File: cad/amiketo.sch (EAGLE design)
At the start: 58 parts, among them CN1 MICROSDPLAIN, J1 HEADER-5X1, Q1 IRLML6344TRPBF, Q2 DMP2035U-7, SW2 SWITCHKMR211, SW3 SWITCHKMR211, U1 STM32F411/48, U2 LSM303D, U3 ADP5062, U4 MCP1824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

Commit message: lis3dh accel
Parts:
- removed C12: 4.7u, jaw:C0603
- removed C13: .22u, jaw:C0603
- U2: value LSM303D -> LIS3DH; device jaw:LSM303D -> jaw:LIS3DH
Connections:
- removed net N$1: C12.P$1, U2.C1
- removed net N$2: C13.P$2, U2.SETP
- removed net N$4: C13.P$1, U2.SETC
- net GND: no longer C12.P$2
- net VCC: now also U2.VCC; no longer U2.VDD
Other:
- moved on the sheet: U2
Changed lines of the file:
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@@
 <part name="U$2" library="adafruit" deviceset="FIDUCIAL" device=""/>
 <part name="U$3" library="adafruit" deviceset="FIDUCIAL" device=""/>
-<part name="C12" library="jaw" deviceset="C" device="0603" value="4.7u"/>
-<part name="C13" library="jaw" deviceset="C" device="0603" value=".22u"/>
 <part name="C14" library="jaw" deviceset="C" device="0603" value=".1u"/>
 <part name="GND12" library="jaw" deviceset="PWR-GND" device=""/>
@@
 <part name="B1" library="jaw" deviceset="BATTERY" device="-CR2016"/>
 <part name="X1" library="jaw" deviceset="RESONATOR" device="CTCE" value="12MHz"/>
-<part name="U2" library="jaw" deviceset="LSM303D" device=""/>
 <part name="U5" library="jaw" deviceset="MAX17048" device=""/>
 <part name="LOGO1" library="Sparkfun-Aesthetics" deviceset="OSHW-LOGO" device="M"/>
@@
 <part name="C6" library="jaw" deviceset="C" device="0603" value="1u"/>
 <part name="C7" library="jaw" deviceset="C" device="0603" value="1u"/>
+<part name="U2" library="jaw" deviceset="LIS3DH" device=""/>
 </parts>
 <sheets>
@@
 <instance part="U$2" gate="G$1" x="269.24" y="40.64"/>
 <instance part="U$3" gate="G$1" x="261.62" y="40.64"/>
-<instance part="C12" gate="G$1" x="127" y="109.22" rot="R90"/>
-<instance part="C13" gate="G$1" x="124.46" y="101.6" rot="R90"/>
 <instance part="C14" gate="G$1" x="132.08" y="119.38"/>
 <instance part="GND12" gate="G$1" x="99.06" y="81.28"/>
@@
 <instance part="B1" gate="G$1" x="226.06" y="170.18"/>
 <instance part="X1" gate="G$1" x="144.78" y="160.02"/>
-<instance part="U2" gate="G$1" x="99.06" y="106.68"/>
 <instance part="U5" gate="G$1" x="127" y="25.4"/>
 <instance part="LOGO1" gate="G$1" x="203.2" y="45.72"/>
@@
 <instance part="C6" gate="G$1" x="226.06" y="73.66"/>
 <instance part="C7" gate="G$1" x="226.06" y="165.1" rot="R270"/>
+<instance part="U2" gate="G$1" x="99.06" y="106.68"/>
 </instances>
 <busses>
@@
 <pinref part="GND12" gate="G$1" pin="GND"/>
 <wire x1="99.06" y1="88.9" x2="99.06" y2="86.36" width="0.1524" layer="91"/>
+<wire x1="99.06" y1="86.36" x2="99.06" y2="83.82" width="0.1524" layer="91"/>
 <pinref part="U2" gate="G$1" pin="GND"/>
-<wire x1="99.06" y1="86.36" x2="99.06" y2="83.82" width="0.1524" layer="91"/>
-<junction x="99.06" y="86.36"/>
-</segment>
-<segment>
-<pinref part="C12" gate="G$1" pin="P$2"/>
-<wire x1="129.54" y1="109.22" x2="132.08" y2="109.22" width="0.1524" layer="91"/>
+<wire x1="99.06" y1="88.9" x2="99.06" y2="91.44" width="0.1524" layer="91"/>
+</segment>
+<segment>
 <wire x1="132.08" y1="109.22" x2="132.08" y2="96.52" width="0.1524" layer="91"/>
 <pinref part="GND14" gate="G$1" pin="GND"/>
 <wire x1="132.08" y1="96.52" x2="132.08" y2="88.9" width="0.1524" layer="91"/>
 <wire x1="132.08" y1="114.3" x2="132.08" y2="109.22" width="0.1524" layer="91"/>
-<junction x="132.08" y="109.22"/>
 <pinref part="C14" gate="G$1" pin="P$2"/>
 <wire x1="132.08" y1="116.84" x2="132.08" y2="114.3" width="0.1524" layer="91"/>
@@
 </segment>
 <segment>
-<pinref part="U2" gate="G$1" pin="SA0"/>
-<wire x1="81.28" y1="96.52" x2="76.2" y2="96.52" width="0.1524" layer="91"/>
-<label x="73.66" y="96.52" size="1.27" layer="95"/>
-</segment>
-<segment>
 <pinref part="U5" gate="G$1" pin="QSTRT"/>
 <wire x1="142.24" y1="22.86" x2="147.32" y2="22.86" width="0.1524" layer="91"/>
@@
 <pinref part="GND24" gate="G$1" pin="GND"/>
 <wire x1="264.16" y1="68.58" x2="256.54" y2="68.58" width="0.1524" layer="91"/>
+</segment>
+<segment>
+<pinref part="U2" gate="G$1" pin="SA0"/>
+<wire x1="83.82" y1="109.22" x2="78.74" y2="109.22" width="0.1524" layer="91"/>
+<label x="73.66" y="109.22" size="1.27" layer="95"/>
 </segment>
 </net>
@@
 <junction x="99.06" y="127"/>
 <pinref part="U2" gate="G$1" pin="VDDIO"/>
-<junction x="96.52" y="127"/>
-<pinref part="U2" gate="G$1" pin="VDD"/>
+<wire x1="101.6" y1="124.46" x2="101.6" y2="121.92" width="0.1524" layer="91"/>
+<pinref part="U2" gate="G$1" pin="VCC"/>
+<wire x1="96.52" y1="124.46" x2="96.52" y2="121.92" width="0.1524" layer="91"/>
 </segment>
 <segment>
@@
 <label x="246.38" y="177.8" size="1.27" layer="95"/>
 <pinref part="J1" gate="G$1" pin="1"/>
-</segment>
-<segment>
-<pinref part="U2" gate="G$1" pin="CS"/>
-<wire x1="81.28" y1="116.84" x2="76.2" y2="116.84" width="0.1524" layer="91"/>
-<label x="73.66" y="116.84" size="1.27" layer="95"/>
 </segment>
 <segment>
@@
 <wire x1="139.7" y1="78.74" x2="139.7" y2="76.2" width="0.1524" layer="91"/>
 <wire x1="139.7" y1="76.2" x2="142.24" y2="76.2" width="0.1524" layer="91"/>
+</segment>
+<segment>
+<pinref part="U2" gate="G$1" pin="CS"/>
+<wire x1="114.3" y1="104.14" x2="119.38" y2="104.14" width="0.1524" layer="91"/>
+<label x="119.38" y="104.14" size="1.27" layer="95"/>
 </segment>
 </net>
@@
 </segment>
 <segment>
-<pinref part="U2" gate="G$1" pin="SCL"/>
-<wire x1="81.28" y1="111.76" x2="76.2" y2="111.76" width="0.1524" layer="91"/>
-<label x="73.66" y="111.76" size="1.27" layer="95"/>
-</segment>
-<segment>
 <pinref part="U5" gate="G$1" pin="SCL"/>
 <wire x1="142.24" y1="27.94" x2="147.32" y2="27.94" width="0.1524" layer="91"/>
@@
 <label x="243.84" y="101.6" size="1.27" layer="95"/>
 </segment>
+<segment>
+<pinref part="U2" gate="G$1" pin="SCL"/>
+<wire x1="83.82" y1="114.3" x2="78.74" y2="114.3" width="0.1524" layer="91"/>
+<label x="73.66" y="114.3" size="1.27" layer="95"/>
+</segment>
 </net>
 <net name="I2CDA" class="0">
@@
 </segment>
 <segment>
-<pinref part="U2" gate="G$1" pin="SDA"/>
-<wire x1="81.28" y1="109.22" x2="76.2" y2="109.22" width="0.1524" layer="91"/>
-<label x="73.66" y="109.22" size="1.27" layer="95"/>
-</segment>
-<segment>
 <pinref part="U5" gate="G$1" pin="SDA"/>
 <wire x1="142.24" y1="30.48" x2="147.32" y2="30.48" width="0.1524" layer="91"/>
@@
 <label x="243.84" y="99.06" size="1.27" layer="95"/>
 </segment>
+<segment>
+<pinref part="U2" gate="G$1" pin="SDA"/>
+<wire x1="83.82" y1="111.76" x2="78.74" y2="111.76" width="0.1524" layer="91"/>
+<label x="73.66" y="111.76" size="1.27" layer="95"/>
+</segment>
 </net>
 <net name="DPYDC" class="0">
@@
 <segment>
 <pinref part="U2" gate="G$1" pin="INT1"/>
-<wire x1="81.28" y1="101.6" x2="76.2" y2="101.6" width="0.1524" layer="91"/>
-<label x="73.66" y="101.6" size="1.27" layer="95"/>
+<wire x1="114.3" y1="109.22" x2="119.38" y2="109.22" width="0.1524" layer="91"/>
+<label x="119.38" y="109.22" size="1.27" layer="95"/>
 </segment>
 </net>
@@
 </segment>
 </net>
-<net name="N$1" class="0">
-<segment>
-<pinref part="C12" gate="G$1" pin="P$1"/>
-<pinref part="U2" gate="G$1" pin="C1"/>
-<wire x1="121.92" y1="109.22" x2="114.3" y2="109.22" width="0.1524" layer="91"/>
-</segment>
-</net>
-<net name="N$2" class="0">
-<segment>
-<pinref part="U2" gate="G$1" pin="SETP"/>
-<wire x1="114.3" y1="106.68" x2="127" y2="106.68" width="0.1524" layer="91"/>
-<pinref part="C13" gate="G$1" pin="P$2"/>
-<wire x1="127" y1="106.68" x2="127" y2="101.6" width="0.1524" layer="91"/>
-</segment>
-</net>
-<net name="N$4" class="0">
-<segment>
-<pinref part="C13" gate="G$1" pin="P$1"/>
-<wire x1="119.38" y1="101.6" x2="116.84" y2="101.6" width="0.1524" layer="91"/>
-<wire x1="116.84" y1="101.6" x2="116.84" y2="104.14" width="0.1524" layer="91"/>
-<pinref part="U2" gate="G$1" pin="SETC"/>
-<wire x1="116.84" y1="104.14" x2="114.3" y2="104.14" width="0.1524" layer="91"/>
-</segment>
-</net>

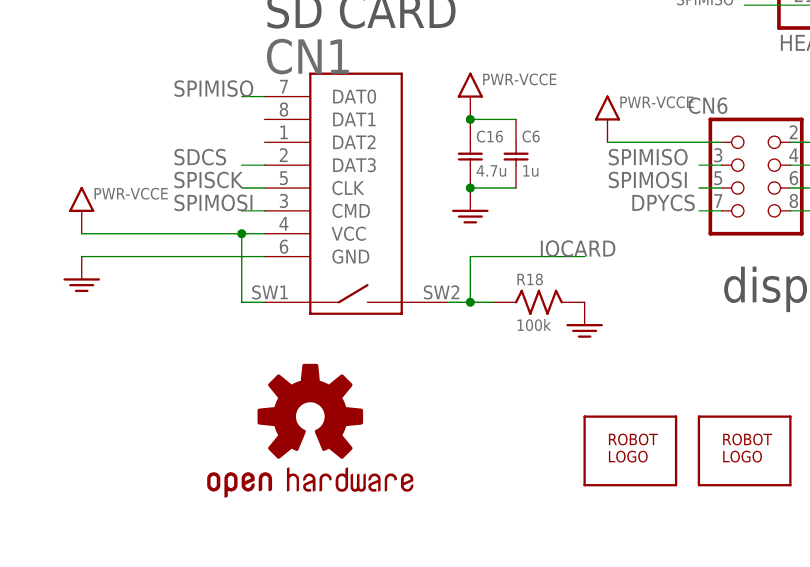
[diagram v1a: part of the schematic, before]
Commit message: move usb, embiggen sd
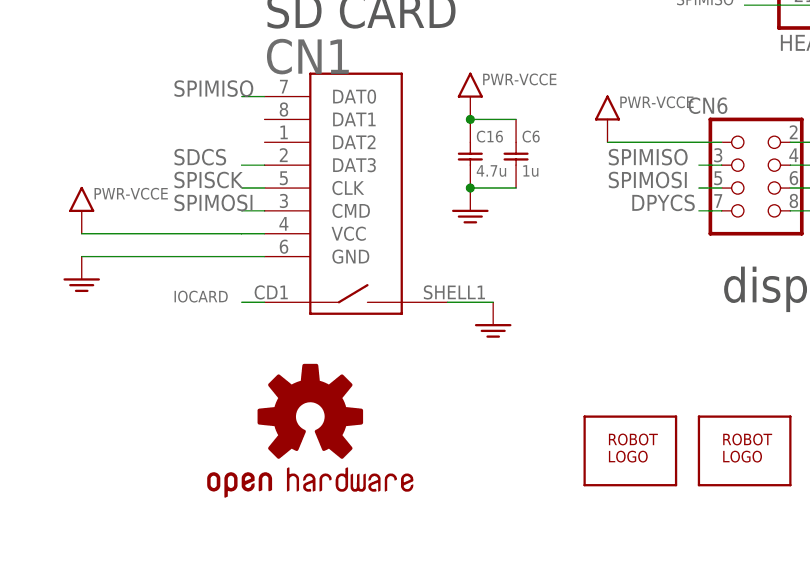
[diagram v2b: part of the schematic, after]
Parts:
- removed R18: 100k, jaw:R0603
- CN1: value MICROSDPLAIN -> MICROSD-EJECT; device jaw:MICROSDPLAIN -> jaw:MICROSD-EJECT
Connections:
- net GND: now also CN1.SW2; no longer R18.P$2
- net IOCARD: now also CN1.SW1; no longer CN1.SW2, R18.P$1
- net VCCE: no longer CN1.SW1
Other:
- moved on the sheet: CN1
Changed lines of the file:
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@@
 <part name="GND10" library="jaw" deviceset="PWR-GND" device=""/>
 <part name="Q1" library="jaw" deviceset="MOSFET" device="SOT-23" value="IRLML6344TRPBF"/>
-<part name="CN1" library="jaw" deviceset="MICROSD" device="PLAIN"/>
+<part name="CN1" library="jaw" deviceset="MICROSD" device="-EJECT" value="MICROSD-EJECT"/>
 <part name="GND22" library="jaw" deviceset="PWR-GND" device=""/>
 <part name="C16" library="jaw" deviceset="C" device="0603" value="4.7u"/>
 <part name="GND23" library="jaw" deviceset="PWR-GND" device=""/>
-<part name="R18" library="jaw" deviceset="R" device="0603" value="100k"/>
 <part name="GND13" library="jaw" deviceset="PWR-GND" device=""/>
 <part name="U$2" library="adafruit" deviceset="FIDUCIAL" device=""/>
@@
 <instance part="C16" gate="G$1" x="220.98" y="73.66"/>
 <instance part="GND23" gate="G$1" x="220.98" y="68.58"/>
-<instance part="R18" gate="G$1" x="228.6" y="58.42"/>
-<instance part="GND13" gate="G$1" x="233.68" y="55.88"/>
+<instance part="GND13" gate="G$1" x="223.52" y="55.88"/>
 <instance part="U$2" gate="G$1" x="269.24" y="40.64"/>
 <instance part="U$3" gate="G$1" x="261.62" y="40.64"/>
@@
 </segment>
 <segment>
-<pinref part="R18" gate="G$1" pin="P$2"/>
-<pinref part="GND13" gate="G$1" pin="GND"/>
-</segment>
-<segment>
 <pinref part="GND9" gate="G$1" pin="GND"/>
 <pinref part="LED1" gate="G$1" pin="C"/>
@@
 <wire x1="83.82" y1="109.22" x2="78.74" y2="109.22" width="0.1524" layer="91"/>
 <label x="73.66" y="109.22" size="1.27" layer="95"/>
+</segment>
+<segment>
+<pinref part="CN1" gate="G$1" pin="SW2"/>
+<pinref part="GND13" gate="G$1" pin="GND"/>
+<wire x1="218.44" y1="58.42" x2="223.52" y2="58.42" width="0.1524" layer="91"/>
 </segment>
 </net>
@@
 <net name="IOCARD" class="0">
 <segment>
-<pinref part="CN1" gate="G$1" pin="SW2"/>
-<pinref part="R18" gate="G$1" pin="P$1"/>
-<wire x1="218.44" y1="58.42" x2="220.98" y2="58.42" width="0.1524" layer="91"/>
-<wire x1="220.98" y1="58.42" x2="223.52" y2="58.42" width="0.1524" layer="91"/>
-<wire x1="220.98" y1="58.42" x2="220.98" y2="63.5" width="0.1524" layer="91"/>
-<junction x="220.98" y="58.42"/>
-<wire x1="220.98" y1="63.5" x2="233.68" y2="63.5" width="0.1524" layer="91"/>
-<label x="228.6" y="63.5" size="1.778" layer="95"/>
-</segment>
-<segment>
 <pinref part="U1" gate="G$1" pin="PA15"/>
 <wire x1="193.04" y1="124.46" x2="198.12" y2="124.46" width="0.1524" layer="91"/>
 <label x="198.12" y="124.46" size="1.27" layer="95"/>
+</segment>
+<segment>
+<pinref part="CN1" gate="G$1" pin="SW1"/>
+<wire x1="198.12" y1="58.42" x2="195.58" y2="58.42" width="0.1524" layer="91"/>
+<label x="187.96" y="58.42" size="1.27" layer="95"/>
 </segment>
 </net>
@@
 <pinref part="CN1" gate="G$1" pin="VCC"/>
 <wire x1="177.8" y1="66.04" x2="195.58" y2="66.04" width="0.1524" layer="91"/>
-<pinref part="CN1" gate="G$1" pin="SW1"/>
 <wire x1="195.58" y1="66.04" x2="198.12" y2="66.04" width="0.1524" layer="91"/>
-<wire x1="198.12" y1="58.42" x2="195.58" y2="58.42" width="0.1524" layer="91"/>
-<wire x1="195.58" y1="58.42" x2="195.58" y2="66.04" width="0.1524" layer="91"/>
-<junction x="195.58" y="66.04"/>
 <pinref part="VCCE2" gate="G$1" pin="VCCE"/>
 </segment>

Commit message: 22pin connector
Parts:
- added C12: .1u, jaw:C0603
- JP1: value HEADER-21X1 -> HEADER-22X1-PTH; device jaw:HEADER-21X1 -> jaw:HEADER-22X1-PTH
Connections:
- net BOOT0: now also JP1.16; no longer JP1.15
- net GND: now also C12.P$2, JP1.13; no longer JP1.12
- net I2CCL: now also JP1.18; no longer JP1.17
- net I2CDA: now also JP1.19; no longer JP1.18
- net NRST: now also JP1.17; no longer JP1.16
- net RX: now also JP1.14; no longer JP1.13
- net SPIMISO: now also JP1.22; no longer JP1.21
- net SPIMOSI: now also JP1.21; no longer JP1.20
- net SPISCK: now also JP1.20; no longer JP1.19
- net TX: now also JP1.15; no longer JP1.14
- net VCC: now also C12.P$1
- net VUSB: now also JP1.12

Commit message: tweak, silk
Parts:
- C6: value 1u -> .1u
- F1: value (none) -> FUSE; device adafruit:PTCFUSE-1206 -> jaw:FUSE
- renumbered NOISY1 to SPKR1
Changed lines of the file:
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@@
 <part name="USB1" library="dp_devices" deviceset="CON-USB-F" device="-MICRO-B"/>
 <part name="CN3" library="adafruit" deviceset="JST_2PIN" device="-SMT-RA"/>
-<part name="F1" library="adafruit" deviceset="PTCFUSE" device="-1206"/>
+<part name="F1" library="jaw" deviceset="FUSE" device=""/>
 <part name="C1" library="jaw" deviceset="C" device="0603" value="10u"/>
 <part name="C2" library="jaw" deviceset="C" device="0603" value="1u"/>
@@
 <part name="R8" library="jaw" deviceset="R" device="0603" value="470"/>
 <part name="GND9" library="jaw" deviceset="PWR-GND" device=""/>
-<part name="NOISY1" library="jaw" deviceset="PUI-5040" device=""/>
+<part name="SPKR1" library="jaw" deviceset="PUI-5040" device=""/>
 <part name="D1" library="jaw" deviceset="DIODE" device="SOD-323"/>
 <part name="VCC3" library="jaw" deviceset="PWR-VCC" device=""/>
@@
 <part name="VCCE3" library="jaw" deviceset="PWR-VCCE" device=""/>
 <part name="VCCE4" library="jaw" deviceset="PWR-VCCE" device=""/>
-<part name="C6" library="jaw" deviceset="C" device="0603" value="1u"/>
+<part name="C6" library="jaw" deviceset="C" device="0603" value=".1u"/>
 <part name="C7" library="jaw" deviceset="C" device="0603" value="1u"/>
 <part name="U2" library="jaw" deviceset="LIS3DH" device=""/>
@@
 <instance part="USB1" gate="USB" x="25.4" y="180.34"/>
 <instance part="CN3" gate="G$1" x="73.66" y="30.48" rot="R180"/>
-<instance part="F1" gate="G$1" x="50.8" y="180.34"/>
+<instance part="F1" gate="G$1" x="50.8" y="182.88"/>
 <instance part="C1" gate="G$1" x="88.9" y="53.34"/>
 <instance part="C2" gate="G$1" x="139.7" y="53.34"/>
@@
 <instance part="R8" gate="G$1" x="43.18" y="139.7" rot="R270"/>
 <instance part="GND9" gate="G$1" x="43.18" y="114.3"/>
-<instance part="NOISY1" gate="G$1" x="30.48" y="142.24"/>
+<instance part="SPKR1" gate="G$1" x="30.48" y="142.24"/>
 <instance part="D1" gate="G$1" x="20.32" y="142.24" rot="R90"/>
 <instance part="VCC3" gate="G$1" x="27.94" y="157.48"/>
@@
 <instance part="GND23" gate="G$1" x="220.98" y="68.58"/>
 <instance part="GND13" gate="G$1" x="223.52" y="55.88"/>
-<instance part="U$2" gate="G$1" x="269.24" y="40.64"/>
-<instance part="U$3" gate="G$1" x="261.62" y="40.64"/>
+<instance part="U$2" gate="G$1" x="271.78" y="25.4"/>
+<instance part="U$3" gate="G$1" x="271.78" y="33.02"/>
 <instance part="C14" gate="G$1" x="132.08" y="119.38"/>
 <instance part="GND12" gate="G$1" x="99.06" y="81.28"/>
@@
 <instance part="GND11" gate="G$1" x="7.62" y="50.8"/>
 <instance part="GND21" gate="G$1" x="68.58" y="43.18"/>
-<instance part="U$4" gate="G$1" x="251.46" y="40.64"/>
+<instance part="U$4" gate="G$1" x="248.92" y="25.4"/>
 <instance part="B1" gate="G$1" x="226.06" y="170.18"/>
 <instance part="X1" gate="G$1" x="144.78" y="160.02"/>
 <instance part="U5" gate="G$1" x="127" y="25.4"/>
-<instance part="LOGO1" gate="G$1" x="203.2" y="45.72"/>
-<instance part="U$1" gate="G$1" x="238.76" y="40.64"/>
+<instance part="LOGO1" gate="G$1" x="261.62" y="27.94"/>
+<instance part="U$1" gate="G$1" x="236.22" y="25.4"/>
 <instance part="R2" gate="G$1" x="17.78" y="121.92"/>
 <instance part="CN6" gate="A" x="251.46" y="71.12"/>
@@
 </segment>
 <segment>
-<pinref part="NOISY1" gate="G$1" pin="P1"/>
+<pinref part="SPKR1" gate="G$1" pin="P1"/>
 <pinref part="VCC3" gate="G$1" pin="VCC"/>
 <wire x1="27.94" y1="154.94" x2="27.94" y2="152.4" width="0.1524" layer="91"/>
@@
 <segment>
 <pinref part="Q1" gate="G$1" pin="D"/>
-<pinref part="NOISY1" gate="G$1" pin="P2"/>
+<pinref part="SPKR1" gate="G$1" pin="P2"/>
 <wire x1="27.94" y1="129.54" x2="27.94" y2="132.08" width="0.1524" layer="91"/>
 <wire x1="27.94" y1="132.08" x2="20.32" y2="132.08" width="0.1524" layer="91"/>
